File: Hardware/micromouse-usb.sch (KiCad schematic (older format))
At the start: 2 parts

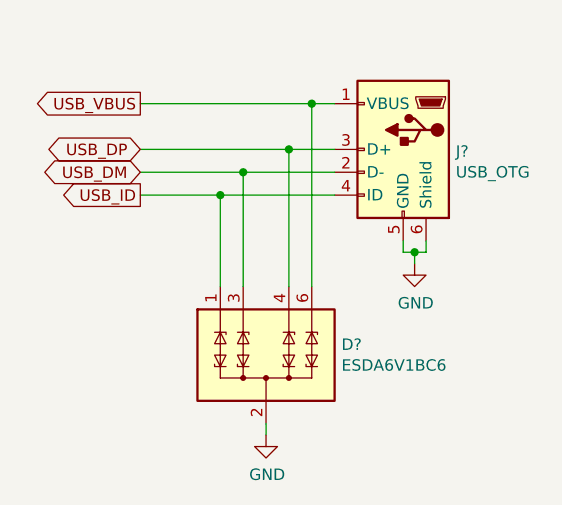
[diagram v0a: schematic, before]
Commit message: add power sub-schematic, fix some supply-connections, rearrange sub-schematics
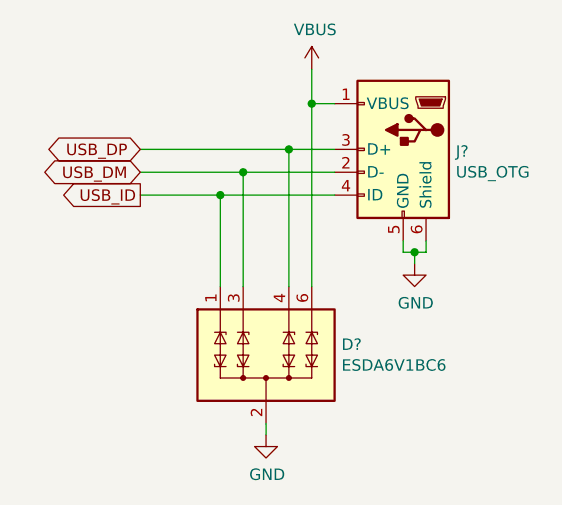
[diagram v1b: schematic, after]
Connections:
- net USB_VBUS renamed VBUS
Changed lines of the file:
@@
 $Descr A4 11693 8268
 encoding utf-8
-Sheet 2 7
+Sheet 2 8
 Title ""
 Date ""
@@
 	-1   0    0    -1
 $EndComp
-Text GLabel 5050 3250 0    50   Output ~ 0
-USB_VBUS
 Text GLabel 5050 3650 0    50   Output ~ 0
 USB_ID
@@
 Text GLabel 5050 3450 0    50   BiDi ~ 0
 USB_DP
-Wire Wire Line
-	5050 3250 5800 3250
 Wire Wire Line
 	5900 3650 5400 3650
@@
 	6300 3900 6300 3850
 Connection ~ 6250 3900
+$Comp
+L power:VBUS #PWR?
+U 1 1 5C8B0F04
+P 5800 3100
+F 0 "#PWR?" H 5800 2950 50  0001 C CNN
+F 1 "VBUS" H 5815 3273 50  0000 C CNN
+F 2 "" H 5800 3100 50  0001 C CNN
+F 3 "" H 5800 3100 50  0001 C CNN
+	1    5800 3100
+	1    0    0    -1
+$EndComp
+Wire Wire Line
+	5800 3100 5800 3250
 $EndSCHEMATC
